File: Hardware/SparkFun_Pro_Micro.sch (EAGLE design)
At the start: 43 parts, among them J2 QWIIC_RIGHT_ANGLE, U1 3.3V, U3 32U4, Y2 16MHz

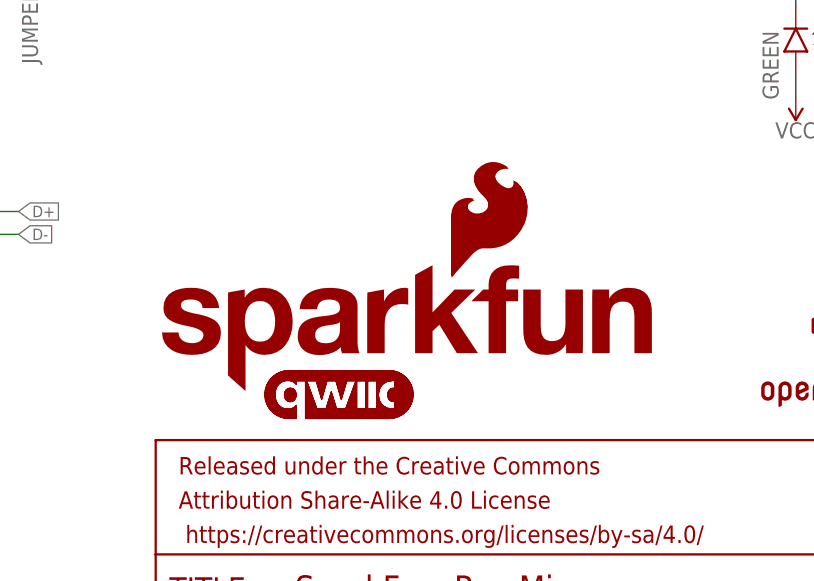
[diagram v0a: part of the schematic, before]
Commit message: Boogie Board Silk Added
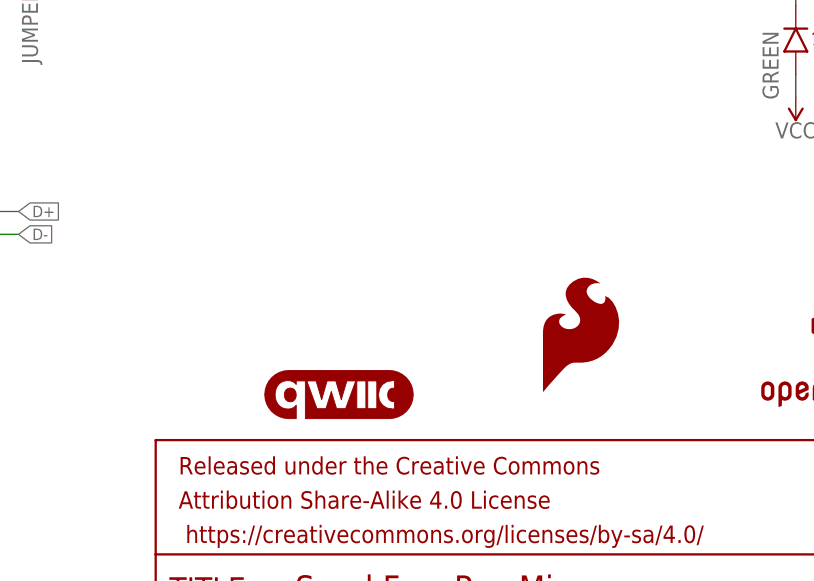
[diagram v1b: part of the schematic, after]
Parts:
- removed LOGO1: SFE_LOGO_NAME_FLAME.1_INCH, SparkFun-Aesthetics:SFE_LOGO_NAME_FLAME.1_INCH
- removed LOGO3: QWIIC_LOGO_6MM, SparkFun-Aesthetics:QWIIC_LOGO_6MM
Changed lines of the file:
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@@
 <drawing>
 <settings>
-<setting alwaysvectorfont="no"/>
+<setting alwaysvectorfont="yes"/>
 <setting keepoldvectorfont="yes"/>
 <setting verticaltext="up"/>
@@
 <part name="S1" library="SparkFun-Switches" deviceset="MOMENTARY-SWITCH-SPST" device="-SMD-4.6X2.8MM" value="Reset"/>
 <part name="GND15" library="SparkFun-PowerSymbols" deviceset="GND" device=""/>
-<part name="LOGO1" library="SparkFun-Aesthetics" deviceset="SFE_LOGO_NAME_FLAME" device=".1_INCH"/>
 <part name="SUPPLY6" library="SparkFun-PowerSymbols" deviceset="V_USB" device=""/>
 <part name="SUPPLY7" library="SparkFun-PowerSymbols" deviceset="V_USB" device=""/>
@@
 <part name="J3" library="Castellated" deviceset="CONN_12" device="CASTLE"/>
 <part name="J4" library="Castellated" deviceset="CONN_12" device="CASTLE"/>
-<part name="LOGO3" library="SparkFun-Aesthetics" deviceset="QWIIC_LOGO" device="_6MM" value="QWIIC_LOGO_6MM"/>
 <part name="R5" library="SparkFun-Resistors" deviceset="2.2KOHM" device="-0402T-1/16W-1%" value="2.2k"/>
 <part name="R7" library="SparkFun-Resistors" deviceset="2.2KOHM" device="-0402T-1/16W-1%" value="2.2k"/>
@@
 <attribute name="VALUE" x="165.1" y="141.986" size="1.778" layer="96" align="top-center"/>
 </instance>
-<instance part="LOGO1" gate="G$1" x="147.32" y="40.64" smashed="yes"/>
 <instance part="SUPPLY6" gate="G$1" x="5.08" y="167.64" smashed="yes">
 <attribute name="VALUE" x="5.08" y="170.434" size="1.778" layer="96" align="bottom-center"/>
@@
 <attribute name="NAME" x="78.74" y="65.532" size="1.778" layer="95" font="vector" rot="R180"/>
 </instance>
-<instance part="LOGO3" gate="G$1" x="167.64" y="40.64" smashed="yes"/>
 <instance part="R5" gate="G$1" x="60.96" y="43.18" smashed="yes" rot="R90">
 <attribute name="NAME" x="59.436" y="43.18" size="1.778" layer="95" font="vector" rot="R90" align="bottom-center"/>
@@
 <attribute name="NAME" x="93.98" y="70.612" size="1.778" layer="95" font="vector" rot="MR180"/>
 </instance>
-<instance part="LOGO4" gate="G$1" x="179.832" y="53.086" smashed="yes"/>
+<instance part="LOGO4" gate="G$1" x="189.992" y="40.386" smashed="yes"/>
 <instance part="JP4" gate="G$1" x="134.62" y="116.84" smashed="yes" rot="R270">
 <attribute name="NAME" x="135.001" y="114.3" size="1.778" layer="95" font="vector" rot="R270"/>
